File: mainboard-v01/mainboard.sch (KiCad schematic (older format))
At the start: 0 parts

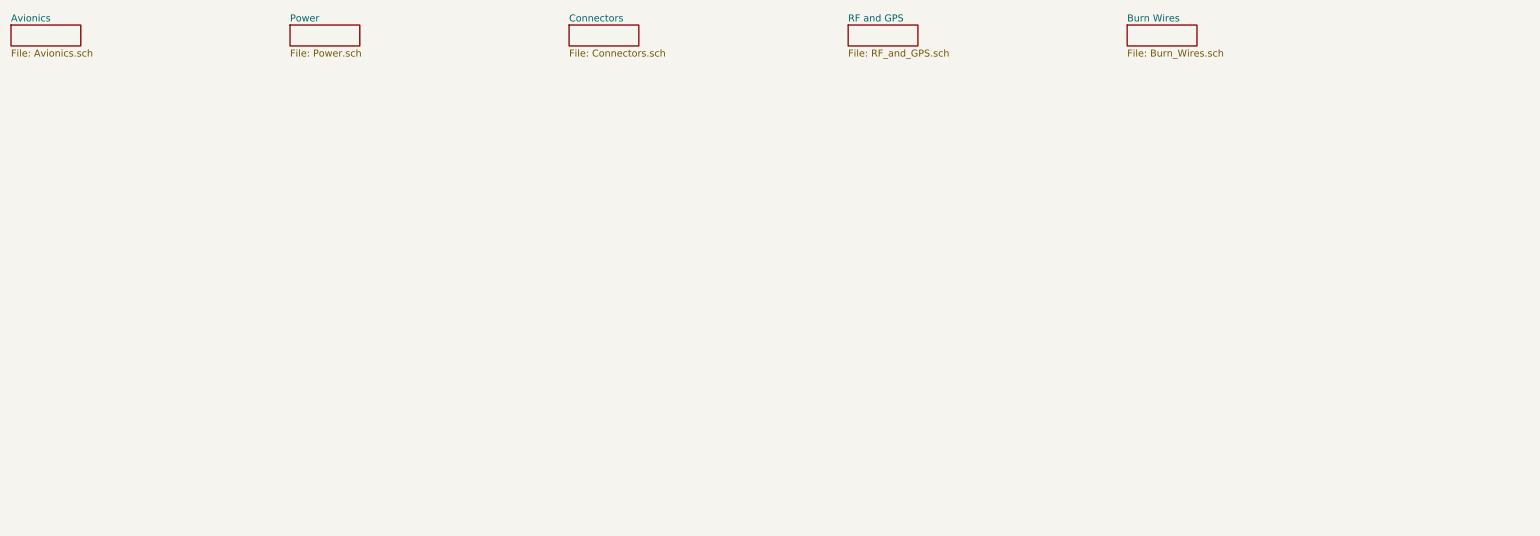
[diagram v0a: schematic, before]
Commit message: adding v01 schematic pdf
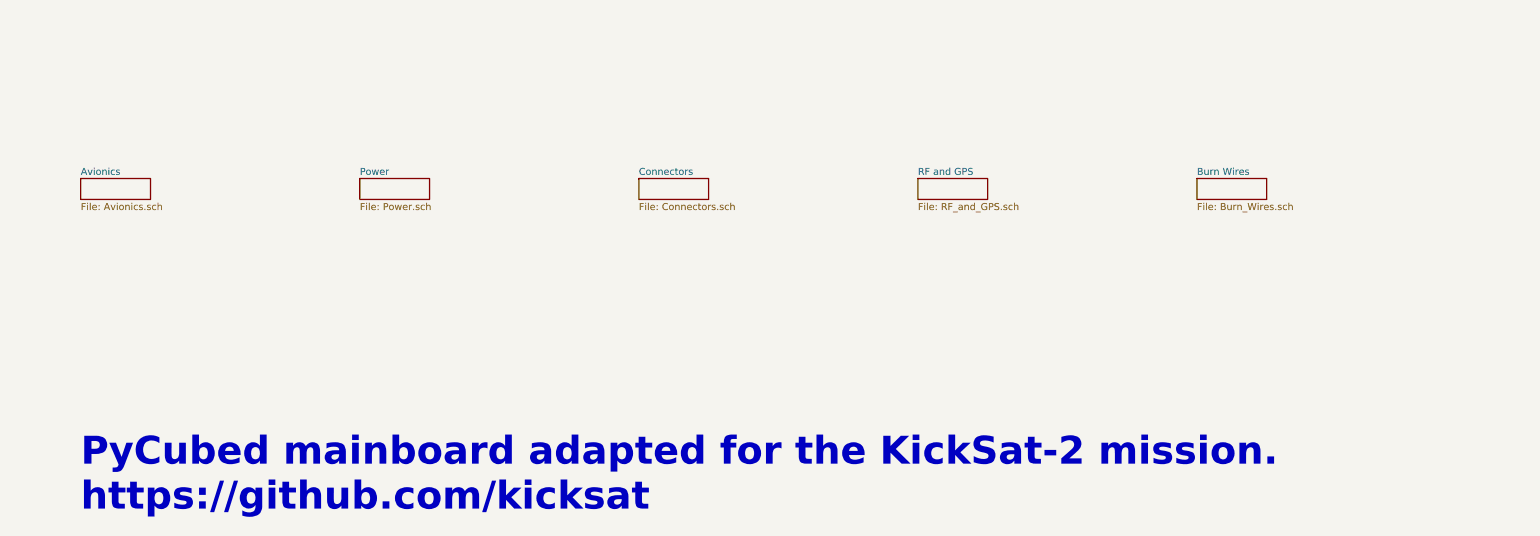
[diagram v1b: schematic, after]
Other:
- note added: "PyCubed mainboard adapted for the KickSat-2 mission.\nhttps://github.com/kicksat"
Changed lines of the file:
@@
 $EndDescr
 $Sheet
-S 1000 1000 500  150
+S 1500 2100 500  150
 U 5CEC5A72
 F0 "Avionics" 50
@@
 $EndSheet
 $Sheet
-S 3000 1000 500  150
+S 3500 2100 500  150
 U 5CEC5DDE
 F0 "Power" 50
@@
 $EndSheet
 $Sheet
-S 5000 1000 500  150
+S 5500 2100 500  150
 U 5CEC60EB
 F0 "Connectors" 50
@@
 $EndSheet
 $Sheet
-S 7000 1000 500  150
+S 7500 2100 500  150
 U 5CEC6281
 F0 "RF and GPS" 50
@@
 $EndSheet
 $Sheet
-S 9000 1000 500  150
+S 9500 2100 500  150
 U 5CEC6476
 F0 "Burn Wires" 50
 F1 "Burn_Wires.sch" 50
 $EndSheet
+Text Notes 1500 4500 0    200  ~ 40
+PyCubed mainboard adapted for the KickSat-2 mission.\nhttps://github.com/kicksat
 $EndSCHEMATC
